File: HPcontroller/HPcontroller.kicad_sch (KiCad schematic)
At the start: 34 parts, among them Q1 Q_Dual_NMOS_S1G1S2G2D2D2D1D1, SW1 SW_SPDT, SW2 SW_SPST, SW3 SW_SPST, SW4 SW_SPST, SW5 SW_SPST, U1 Adafruit_QTPY_ESP32-C3, U2 NCP81071B

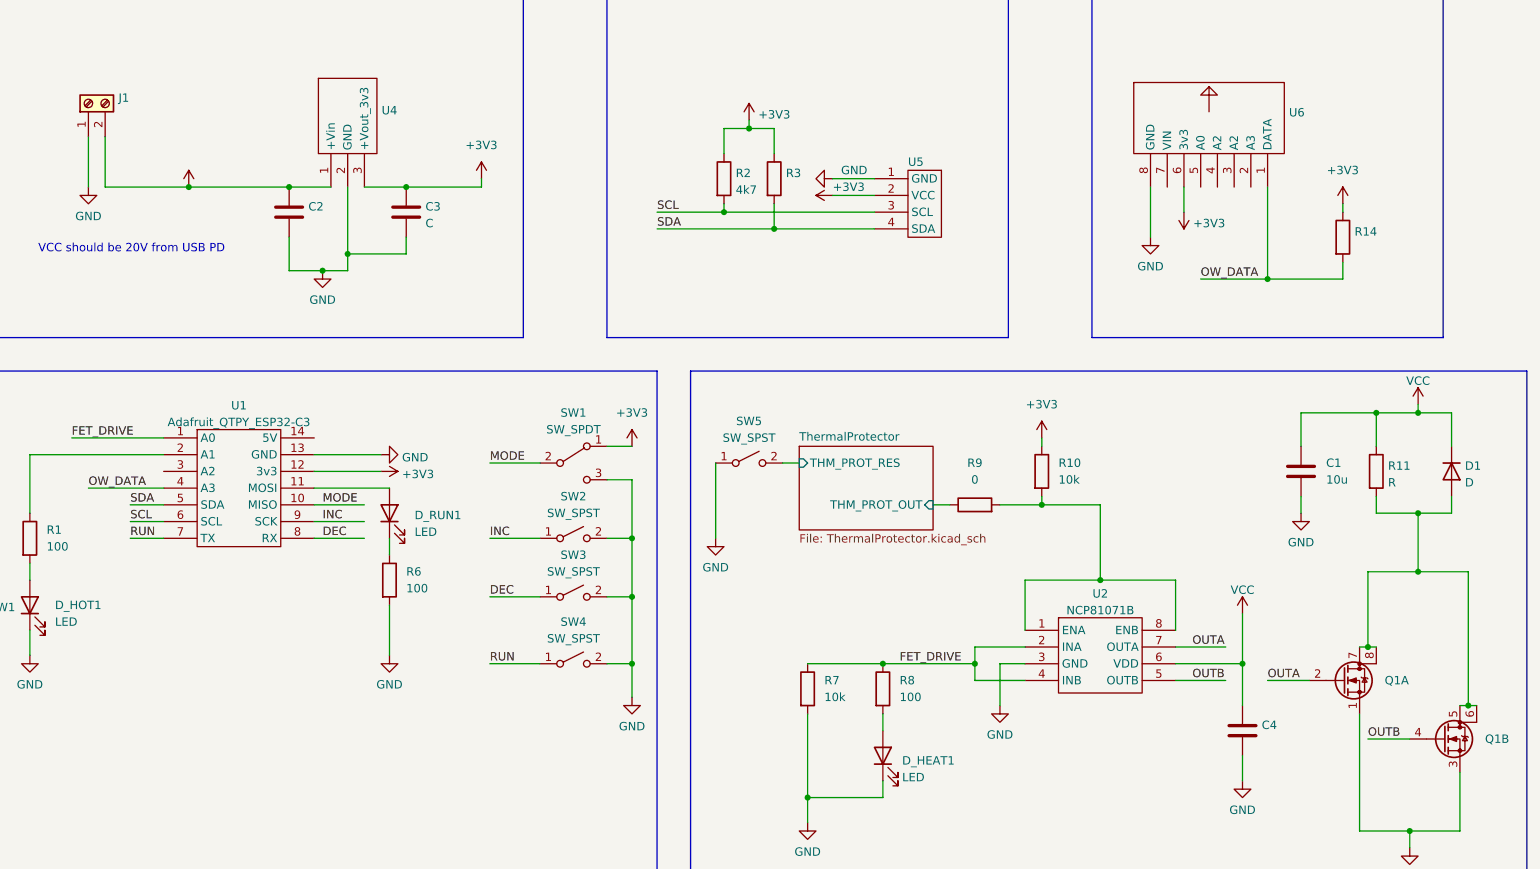
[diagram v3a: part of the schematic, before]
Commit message: routing more.  waitingfor PD trigger to arrive
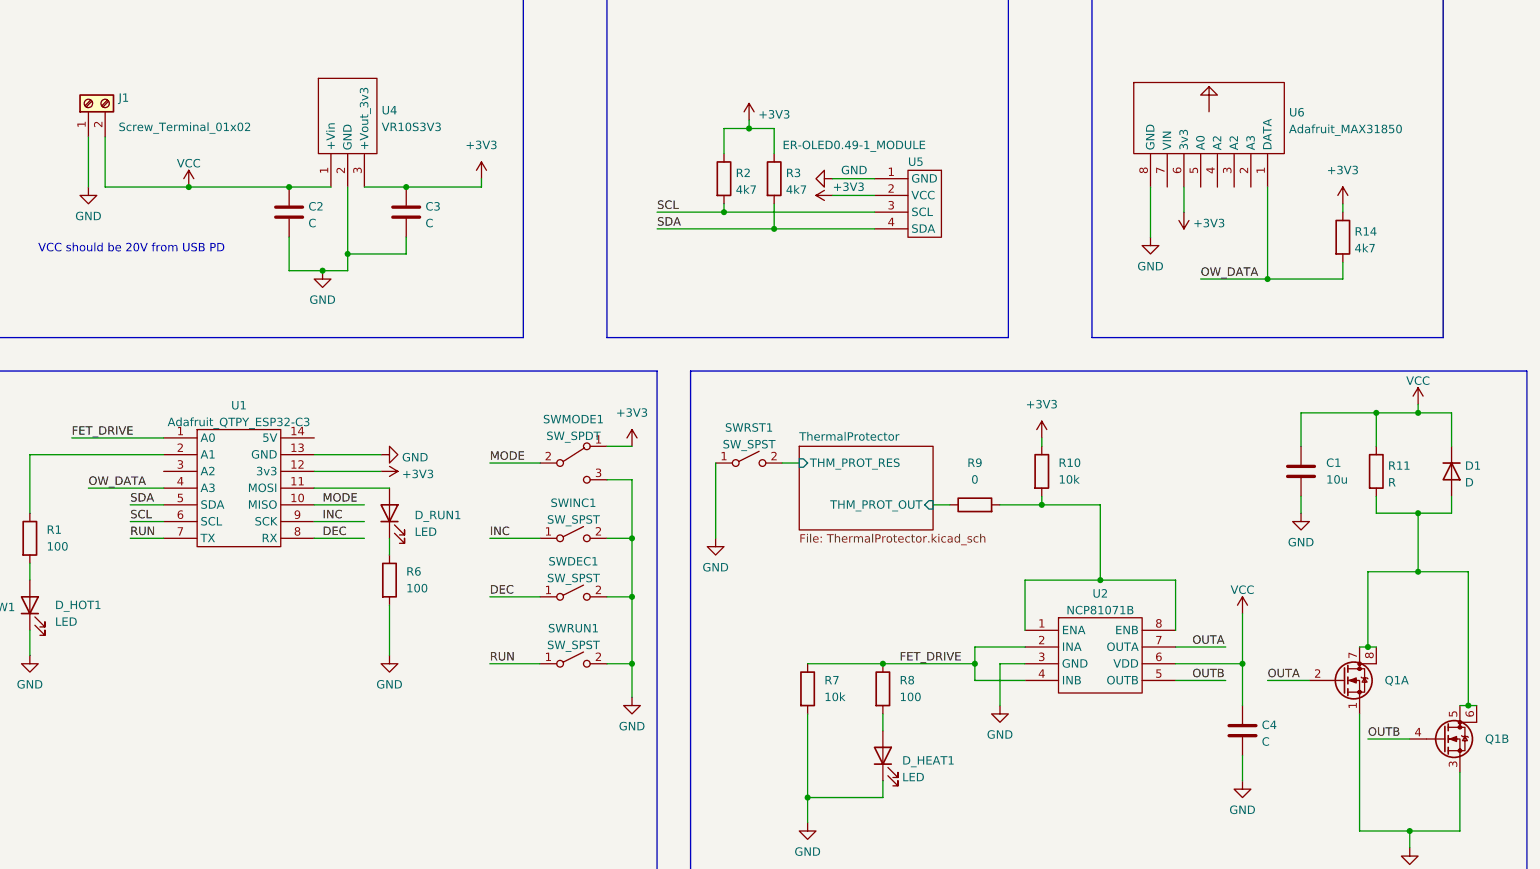
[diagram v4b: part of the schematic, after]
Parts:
- C2, C4: value (none) -> C; footprint (none) -> Capacitor_SMD:C_0805_2012Metric_Pad1.18x1.45mm_HandSolder
- C3: footprint (none) -> Capacitor_SMD:C_0805_2012Metric_Pad1.18x1.45mm_HandSolder
- J1: value (none) -> Screw_Terminal_01x02
- R14, R3: value (none) -> 4k7; footprint (none) -> Resistor_SMD:R_0805_2012Metric_Pad1.20x1.40mm_HandSolder
- R2: footprint (none) -> Resistor_SMD:R_0805_2012Metric_Pad1.20x1.40mm_HandSolder
- U1: footprint (none) -> DevBoards:QTPY ESP32 C3
- U4: value (none) -> VR10S3V3; footprint (none) -> DevBoards:3pinDCDC
- U5: value (none) -> ER-OLED0.49-1_MODULE; footprint (none) -> Connector_PinSocket_2.54mm:PinSocket_1x04_P2.54mm_Vertical
- U6: value (none) -> Adafruit_MAX31850; footprint (none) -> Connector_PinSocket_2.54mm:PinSocket_1x08_P2.54mm_Vertical
- renumbered SW3 to SWDEC1, SW2 to SWINC1, SW1 to SWMODE1, SW5 to SWRST1, SW4 to SWRUN1
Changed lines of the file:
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@@
       (effects (font (size 1.27 1.27)) (justify left))
     )
-    (property "Value" "" (id 1) (at 245.8212 39.4847 0)
-      (effects (font (size 1.27 1.27)) (justify left))
-    )
-    (property "Footprint" "" (id 2) (at 247.65 48.26 90)
+    (property "Value" "Adafruit_MAX31850" (id 1) (at 245.8212 39.4847 0)
+      (effects (font (size 1.27 1.27)) (justify left))
+    )
+    (property "Footprint" "Connector_PinSocket_2.54mm:PinSocket_1x08_P2.54mm_Vertical" (id 2) (at 247.65 48.26 90)
       (effects (font (size 1.27 1.27)) hide)
     )
@@
   (symbol (lib_id "Switch:SW_SPST") (at 137.16 120.65 0) (unit 1)
     (in_bom yes) (on_board yes) (fields_autoplaced)
-    (property "Reference" "SW4" (id 0) (at 137.16 114.3 0))
-    (property "Value" "SW_SPST" (id 1) (at 137.16 116.84 0))
+    (property "Reference" "SWRUN1" (id 0) (at 137.16 115.2992 0))
+    (property "Value" "SW_SPST" (id 1) (at 137.16 117.8361 0))
     (property "Footprint" "Button_Switch_SMD:SW_SPST_PTS645" (id 2) (at 137.16 120.65 0)
       (effects (font (size 1.27 1.27)) hide)
@@
     (property "Reference" "U1" (id 0) (at 86.36 81.441 0))
     (property "Value" "Adafruit_QTPY_ESP32-C3" (id 1) (at 86.36 83.9779 0))
-    (property "Footprint" "" (id 2) (at 74.93 86.36 0)
+    (property "Footprint" "DevBoards:QTPY ESP32 C3" (id 2) (at 74.93 86.36 0)
       (effects (font (size 1.27 1.27)) hide)
     )
@@
   (symbol (lib_id "Switch:SW_SPST") (at 137.16 101.6 0) (unit 1)
     (in_bom yes) (on_board yes) (fields_autoplaced)
-    (property "Reference" "SW2" (id 0) (at 137.16 95.25 0))
-    (property "Value" "SW_SPST" (id 1) (at 137.16 97.79 0))
+    (property "Reference" "SWINC1" (id 0) (at 137.16 96.2492 0))
+    (property "Value" "SW_SPST" (id 1) (at 137.16 98.7861 0))
     (property "Footprint" "Button_Switch_SMD:SW_SPST_PTS645" (id 2) (at 137.16 101.6 0)
       (effects (font (size 1.27 1.27)) hide)
@@
       (effects (font (size 1.27 1.27)) hide)
     )
-    (property "Value" "" (id 1) (at 78.74 44.6842 0))
+    (property "Value" "VCC" (id 1) (at 78.74 44.6842 0))
     (property "Footprint" "" (id 2) (at 78.74 48.26 0)
       (effects (font (size 1.27 1.27)) hide)
@@
       (effects (font (size 1.27 1.27)) (justify left))
     )
-    (property "Value" "" (id 1) (at 241.681 132.5122 0)
-      (effects (font (size 1.27 1.27)) (justify left))
-    )
-    (property "Footprint" "" (id 2) (at 239.7252 134.62 0)
+    (property "Value" "C" (id 1) (at 241.681 132.5122 0)
+      (effects (font (size 1.27 1.27)) (justify left))
+    )
+    (property "Footprint" "Capacitor_SMD:C_0805_2012Metric_Pad1.18x1.45mm_HandSolder" (id 2) (at 239.7252 134.62 0)
       (effects (font (size 1.27 1.27)) hide)
     )
@@
       (effects (font (size 1.27 1.27)) (justify left))
     )
-    (property "Value" "" (id 1) (at 108.0262 39.1672 0)
-      (effects (font (size 1.27 1.27)) (justify left))
-    )
-    (property "Footprint" "" (id 2) (at 102.87 33.655 0)
+    (property "Value" "VR10S3V3" (id 1) (at 108.0262 39.1672 0)
+      (effects (font (size 1.27 1.27)) (justify left))
+    )
+    (property "Footprint" "DevBoards:3pinDCDC" (id 2) (at 102.87 33.655 0)
       (effects (font (size 1.27 1.27)) hide)
     )
@@
       (effects (font (size 1.27 1.27)) (justify left))
     )
-    (property "Value" "" (id 1) (at 255.778 57.5822 0)
-      (effects (font (size 1.27 1.27)) (justify left))
-    )
-    (property "Footprint" "" (id 2) (at 252.222 55.88 90)
+    (property "Value" "4k7" (id 1) (at 255.778 57.5822 0)
+      (effects (font (size 1.27 1.27)) (justify left))
+    )
+    (property "Footprint" "Resistor_SMD:R_0805_2012Metric_Pad1.20x1.40mm_HandSolder" (id 2) (at 252.222 55.88 90)
       (effects (font (size 1.27 1.27)) hide)
     )
@@
       (effects (font (size 1.27 1.27)) (justify left))
     )
-    (property "Footprint" "" (id 2) (at 112.7252 55.88 0)
+    (property "Footprint" "Capacitor_SMD:C_0805_2012Metric_Pad1.18x1.45mm_HandSolder" (id 2) (at 112.7252 55.88 0)
       (effects (font (size 1.27 1.27)) hide)
     )
@@
       (effects (font (size 1.27 1.27)) (justify right))
     )
-    (property "Value" "" (id 1) (at 68.072 39.1672 90)
+    (property "Value" "Screw_Terminal_01x02" (id 1) (at 68.072 39.1672 90)
       (effects (font (size 1.27 1.27)) (justify right))
     )
@@
       (effects (font (size 1.27 1.27)) (justify left))
     )
-    (property "Footprint" "" (id 2) (at 158.242 46.99 90)
+    (property "Footprint" "Resistor_SMD:R_0805_2012Metric_Pad1.20x1.40mm_HandSolder" (id 2) (at 158.242 46.99 90)
       (effects (font (size 1.27 1.27)) hide)
     )
@@
       (effects (font (size 1.27 1.27)) (justify left))
     )
-    (property "Value" "" (id 1) (at 168.91 41.91 90)
-      (effects (font (size 1.27 1.27)) (justify left))
-    )
-    (property "Footprint" "" (id 2) (at 191.135 52.705 0)
+    (property "Value" "ER-OLED0.49-1_MODULE" (id 1) (at 168.91 41.91 90)
+      (effects (font (size 1.27 1.27)) (justify left))
+    )
+    (property "Footprint" "Connector_PinSocket_2.54mm:PinSocket_1x04_P2.54mm_Vertical" (id 2) (at 191.135 52.705 0)
       (effects (font (size 1.27 1.27)) hide)
     )
@@
   (symbol (lib_id "Switch:SW_SPDT") (at 137.16 90.17 0) (unit 1)
     (in_bom yes) (on_board yes) (fields_autoplaced)
-    (property "Reference" "SW1" (id 0) (at 137.16 82.55 0))
-    (property "Value" "SW_SPDT" (id 1) (at 137.16 85.09 0))
+    (property "Reference" "SWMODE1" (id 0) (at 137.16 83.5492 0))
+    (property "Value" "SW_SPDT" (id 1) (at 137.16 86.0861 0))
     (property "Footprint" "Button_Switch_THT:SW_Slide_1P2T_CK_OS102011MS2Q" (id 2) (at 137.16 90.17 0)
       (effects (font (size 1.27 1.27)) hide)
@@
       (effects (font (size 1.27 1.27)) (justify right))
     )
-    (property "Value" "" (id 1) (at 96.901 53.7722 0)
-      (effects (font (size 1.27 1.27)) (justify right))
-    )
-    (property "Footprint" "" (id 2) (at 93.0148 55.88 0)
+    (property "Value" "C" (id 1) (at 96.901 53.7722 0)
+      (effects (font (size 1.27 1.27)) (justify right))
+    )
+    (property "Footprint" "Capacitor_SMD:C_0805_2012Metric_Pad1.18x1.45mm_HandSolder" (id 2) (at 93.0148 55.88 0)
       (effects (font (size 1.27 1.27)) hide)
     )
@@
   (symbol (lib_id "Switch:SW_SPST") (at 137.16 110.49 0) (unit 1)
     (in_bom yes) (on_board yes) (fields_autoplaced)
-    (property "Reference" "SW3" (id 0) (at 137.16 104.14 0))
-    (property "Value" "SW_SPST" (id 1) (at 137.16 106.68 0))
+    (property "Reference" "SWDEC1" (id 0) (at 137.16 105.1392 0))
+    (property "Value" "SW_SPST" (id 1) (at 137.16 107.6761 0))
     (property "Footprint" "Button_Switch_SMD:SW_SPST_PTS645" (id 2) (at 137.16 110.49 0)
       (effects (font (size 1.27 1.27)) hide)
@@
       (effects (font (size 1.27 1.27)) (justify left))
     )
-    (property "Value" "" (id 1) (at 169.418 48.6922 0)
-      (effects (font (size 1.27 1.27)) (justify left))
-    )
-    (property "Footprint" "" (id 2) (at 165.862 46.99 90)
+    (property "Value" "4k7" (id 1) (at 169.418 48.6922 0)
+      (effects (font (size 1.27 1.27)) (justify left))
+    )
+    (property "Footprint" "Resistor_SMD:R_0805_2012Metric_Pad1.20x1.40mm_HandSolder" (id 2) (at 165.862 46.99 90)
       (effects (font (size 1.27 1.27)) hide)
     )
@@
   (symbol (lib_id "Switch:SW_SPST") (at 163.83 90.17 0) (unit 1)
     (in_bom yes) (on_board yes) (fields_autoplaced)
-    (property "Reference" "SW5" (id 0) (at 163.83 83.82 0))
-    (property "Value" "SW_SPST" (id 1) (at 163.83 86.36 0))
+    (property "Reference" "SWRST1" (id 0) (at 163.83 84.8192 0))
+    (property "Value" "SW_SPST" (id 1) (at 163.83 87.3561 0))
     (property "Footprint" "Button_Switch_SMD:SW_SPST_PTS645" (id 2) (at 163.83 90.17 0)
       (effects (font (size 1.27 1.27)) hide)
@@
       (reference "RTHERM1") (unit 1) (value "10kTHERM") (footprint "")
     )
+    (path "/edfb7da0-064d-4a6b-93c6-53ef8dfbaf40"
+      (reference "SWDEC1") (unit 1) (value "SW_SPST") (footprint "Button_Switch_SMD:SW_SPST_PTS645")
+    )
+    (path "/31b26b9b-45e5-44a7-af9d-83cc0724e7a4"
+      (reference "SWINC1") (unit 1) (value "SW_SPST") (footprint "Button_Switch_SMD:SW_SPST_PTS645")
+    )
     (path "/bfced798-567b-4940-880c-a76e32fcc15b"
-      (reference "SW1") (unit 1) (value "SW_SPDT") (footprint "Button_Switch_THT:SW_Slide_1P2T_CK_OS102011MS2Q")
-    )
-    (path "/31b26b9b-45e5-44a7-af9d-83cc0724e7a4"
-      (reference "SW2") (unit 1) (value "SW_SPST") (footprint "Button_Switch_SMD:SW_SPST_PTS645")
-    )
-    (path "/edfb7da0-064d-4a6b-93c6-53ef8dfbaf40"
-      (reference "SW3") (unit 1) (value "SW_SPST") (footprint "Button_Switch_SMD:SW_SPST_PTS645")
+      (reference "SWMODE1") (unit 1) (value "SW_SPDT") (footprint "Button_Switch_THT:SW_Slide_1P2T_CK_OS102011MS2Q")
+    )
+    (path "/fa398d76-e65a-4fec-bd14-a4169f0f303c"
+      (reference "SWRST1") (unit 1) (value "SW_SPST") (footprint "Button_Switch_SMD:SW_SPST_PTS645")
     )
     (path "/0d8bd60d-aa7a-4efb-b7cd-07008c7e6860"
-      (reference "SW4") (unit 1) (value "SW_SPST") (footprint "Button_Switch_SMD:SW_SPST_PTS645")
-    )
-    (path "/fa398d76-e65a-4fec-bd14-a4169f0f303c"
-      (reference "SW5") (unit 1) (value "SW_SPST") (footprint "Button_Switch_SMD:SW_SPST_PTS645")
+      (reference "SWRUN1") (unit 1) (value "SW_SPST") (footprint "Button_Switch_SMD:SW_SPST_PTS645")
     )
     (path "/30288e16-85e4-489c-a76f-2d2e0f53c965"

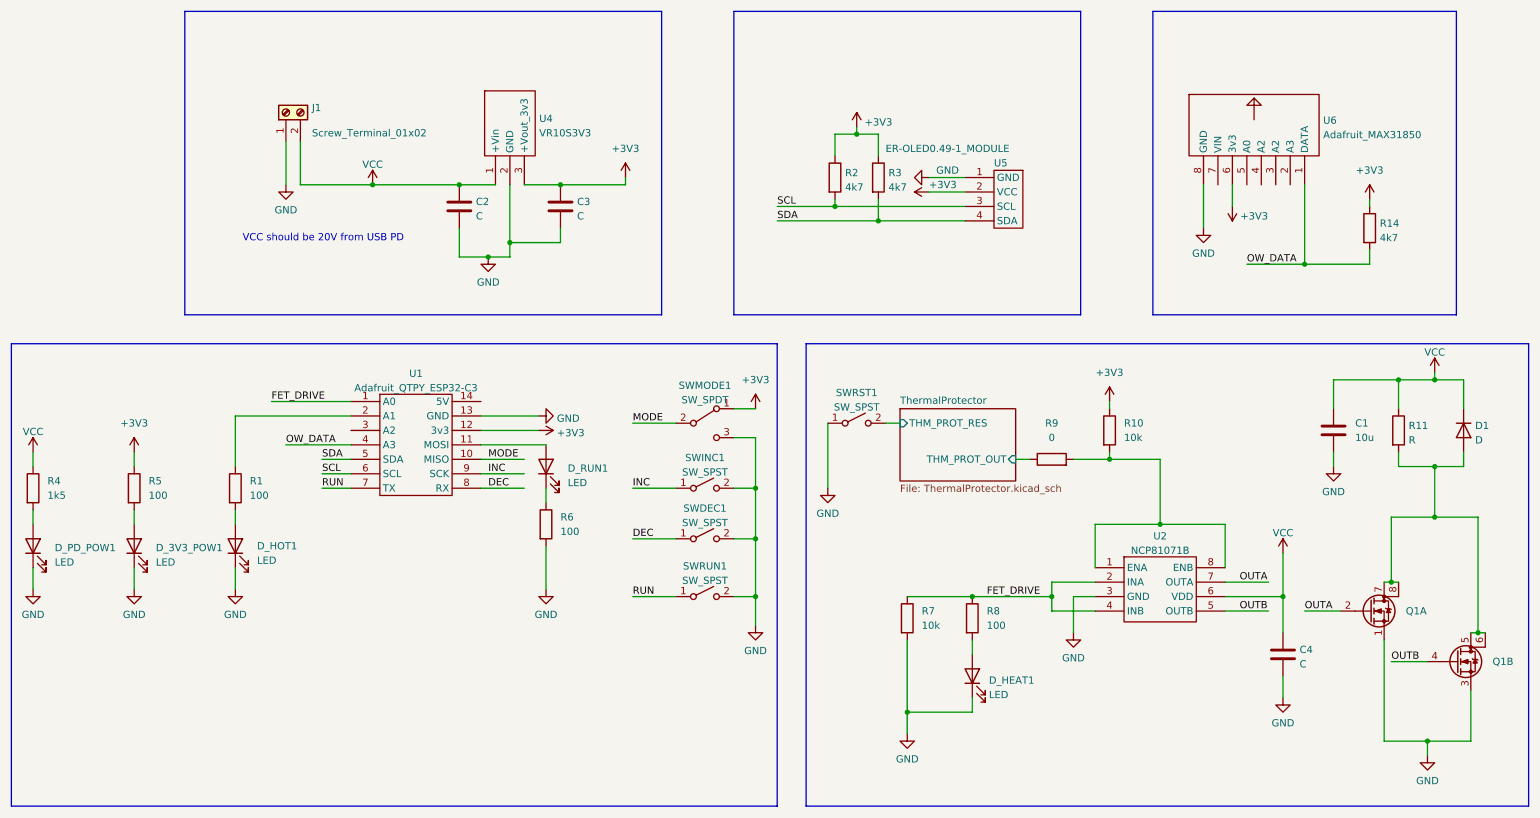
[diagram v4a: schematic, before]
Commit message: minor pcb change to give TC wires more room
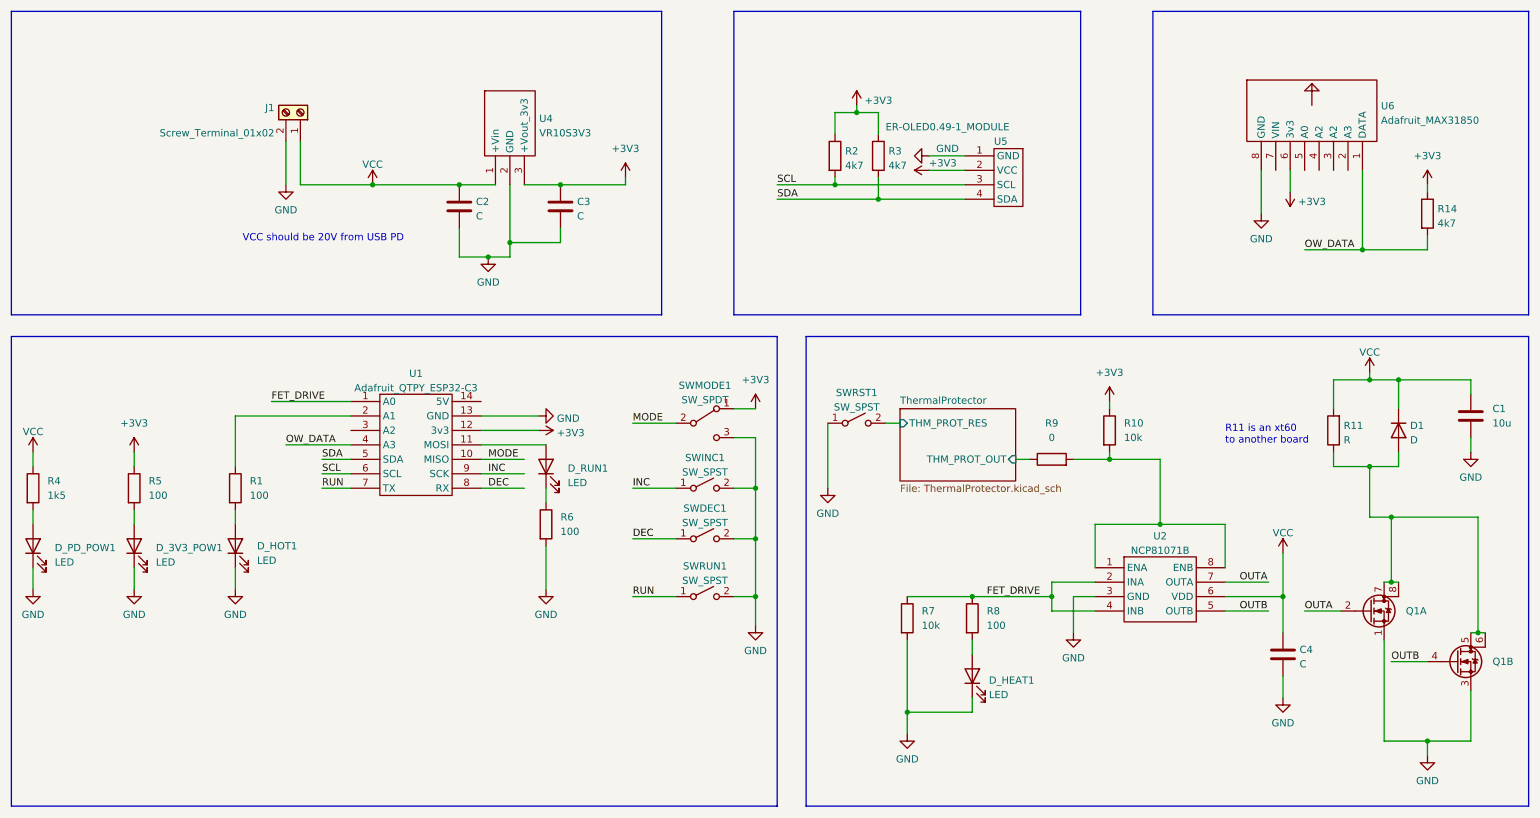
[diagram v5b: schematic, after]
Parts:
- R11: footprint Resistor_SMD:R_0805_2012Metric_Pad1.20x1.40mm_HandSolder -> (none)
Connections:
- net GND: now also J1.2 (Pin_2); no longer J1.1 (Pin_1)
- net VCC: now also J1.1 (Pin_1), R11.2; no longer J1.2 (Pin_2), R11.1
- net at D1.2 (A), Q1.5 (D), Q1.6 (D)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: now also R11.1; no longer R11.2
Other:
- note added: "R11 is an xt60 to another board"
- moved on the sheet: C1, D1, J1, R11, R14, R2, R3, U5, U6
